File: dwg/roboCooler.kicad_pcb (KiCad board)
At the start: 2 copper layers, 36 parts, among them J1 CONN_02X25, J10 CONN_01X12, J11 CONN_01X12, J2 CONN_02X25, J3 CONN_01X04, J5 CONN_01X02, J7 CONN_01X02, Q1 NMOS, Q2 NMOS, Q3 NMOS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

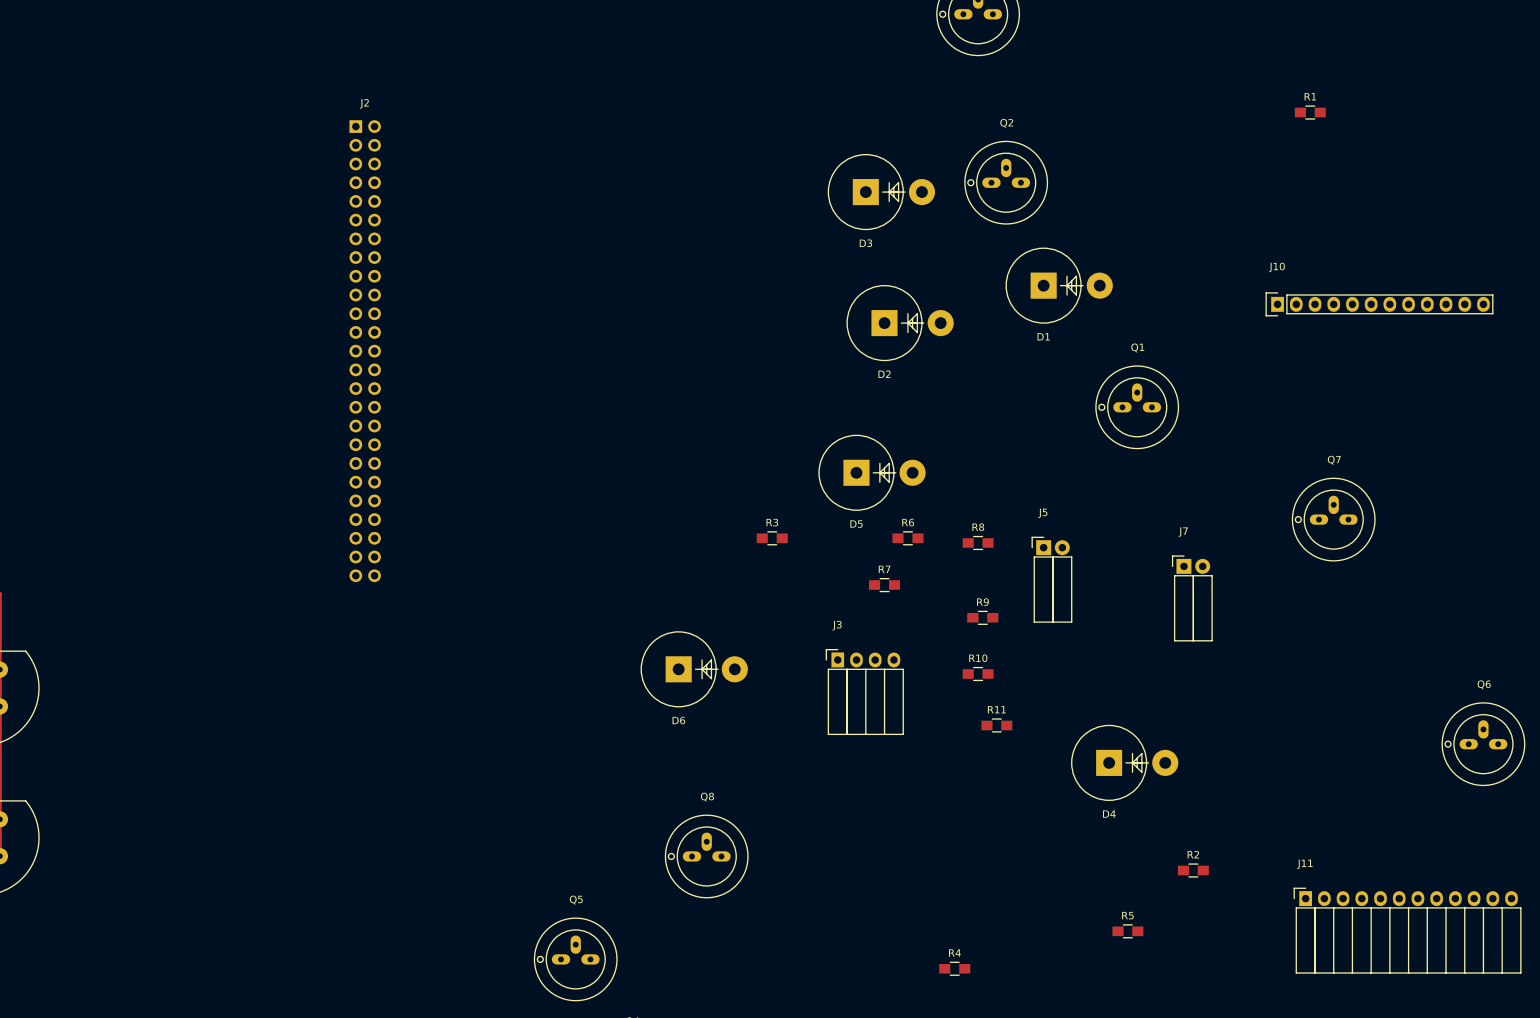
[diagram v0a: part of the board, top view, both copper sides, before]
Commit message: added cap sense to layout
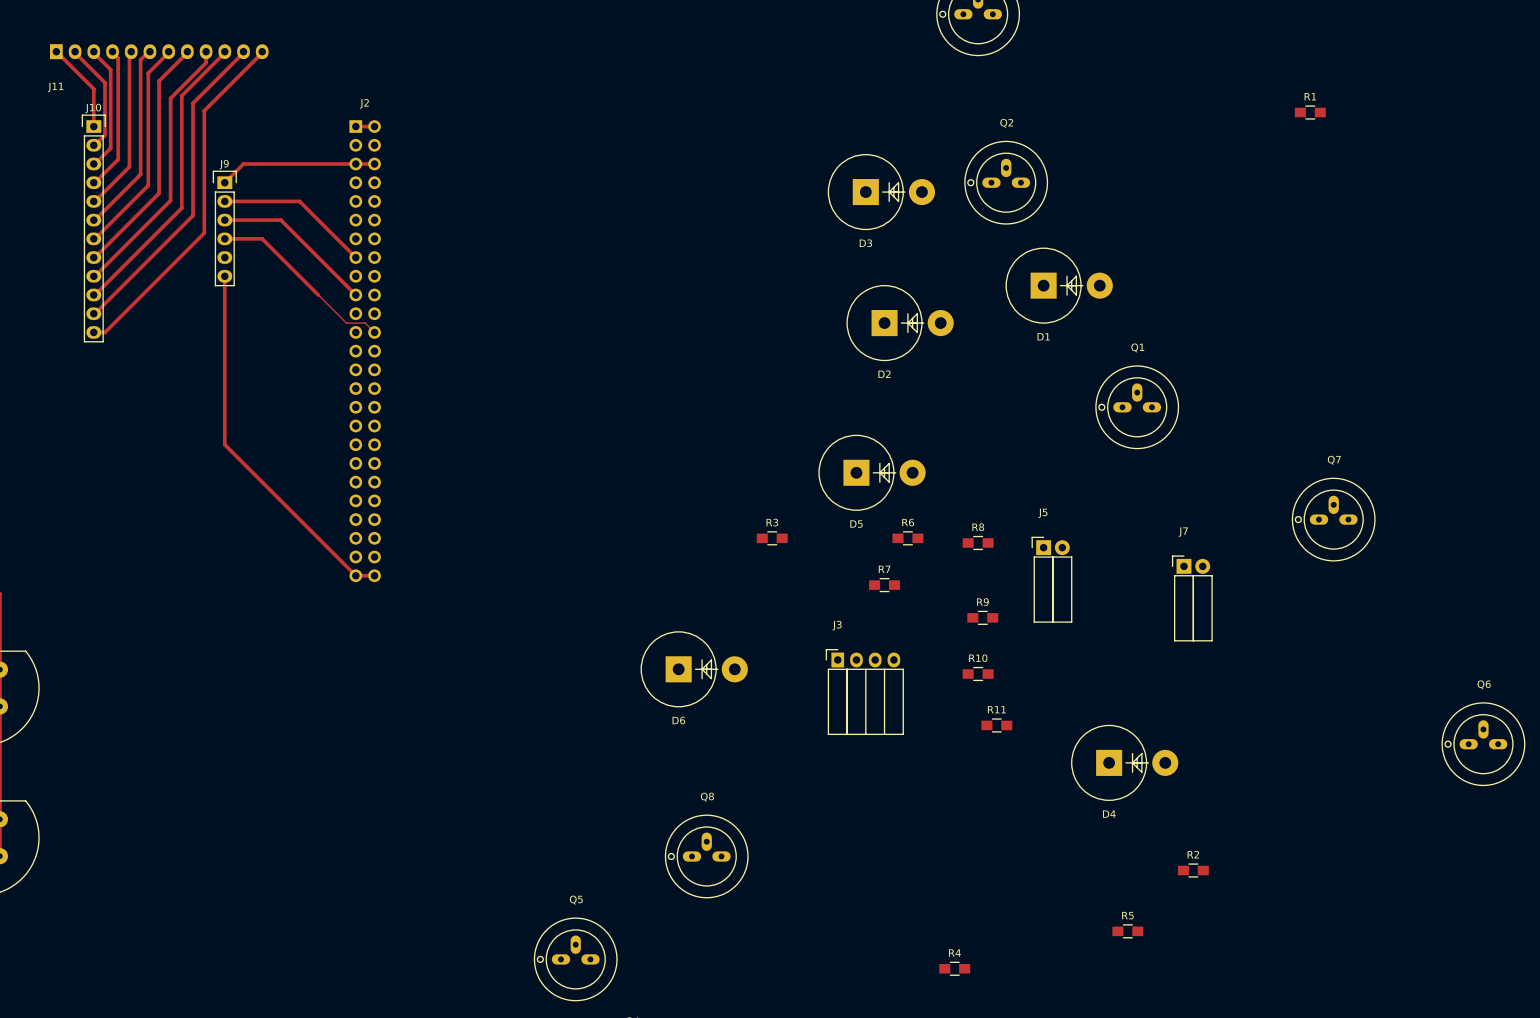
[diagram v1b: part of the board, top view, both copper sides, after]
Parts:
- added J9: CONN_01X06, Pin_Headers:Pin_Header_Straight_1x06, F.Cu at (99.1, 48.3)
- J11: moved to B.Cu
- moved J11 204.8 mm to (76.2, 30.5)
- moved J10 162.5 mm to (81.3, 40.6), turned to 270 degrees
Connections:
- J11 pad 1: Net-(J11-Pad1) -> CS_11
- J11 pad 10: Net-(J11-Pad10) -> CS_2
- J11 pad 11: Net-(J11-Pad11) -> CS_1
- J11 pad 12: Net-(J11-Pad12) -> CS_0
- J11 pad 2: Net-(J11-Pad2) -> CS_10
- J11 pad 3: Net-(J11-Pad3) -> CS_9
- J11 pad 4: Net-(J11-Pad4) -> CS_8
- J11 pad 5: Net-(J11-Pad5) -> CS_7
- J11 pad 6: Net-(J11-Pad6) -> CS_6
- J11 pad 7: Net-(J11-Pad7) -> CS_5
- J11 pad 8: Net-(J11-Pad8) -> CS_4
- J11 pad 9: Net-(J11-Pad9) -> CS_3
- J2 pad 15: Net-(J2-Pad15) -> CS_IRQ
- J2 pad 46: CS_IRQ -> Net-(J2-Pad46)
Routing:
- net POWER_GND: track 41.7 -> 94.8 mm
- net CS_0: track 0.00 -> 48.5 mm
- net CS_1: track 0.00 -> 44.1 mm
- net CS_2: track 0.00 -> 40.5 mm
- net CS_3: track 0.00 -> 36.9 mm
- net CS_4: track 0.00 -> 33.3 mm
- net CS_5: track 0.00 -> 29.7 mm
- net CS_6: track 0.00 -> 26.3 mm
- net CS_SDA: track 0.00 -> 25.6 mm
- net CS_7: track 0.00 -> 22.5 mm
- net CS_SCL: track 0.00 -> 22.0 mm
- net +3V3: track 0.00 -> 21.4 mm
- net CS_IRQ: track 0.00 -> 20.9 mm
- net CS_8: track 0.00 -> 19.6 mm
- net CS_9: track 0.00 -> 17.2 mm
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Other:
- net class BetweenPins added: clearance 0.2, trace_width 0.25, via_dia 0.6, via_drill 0.4

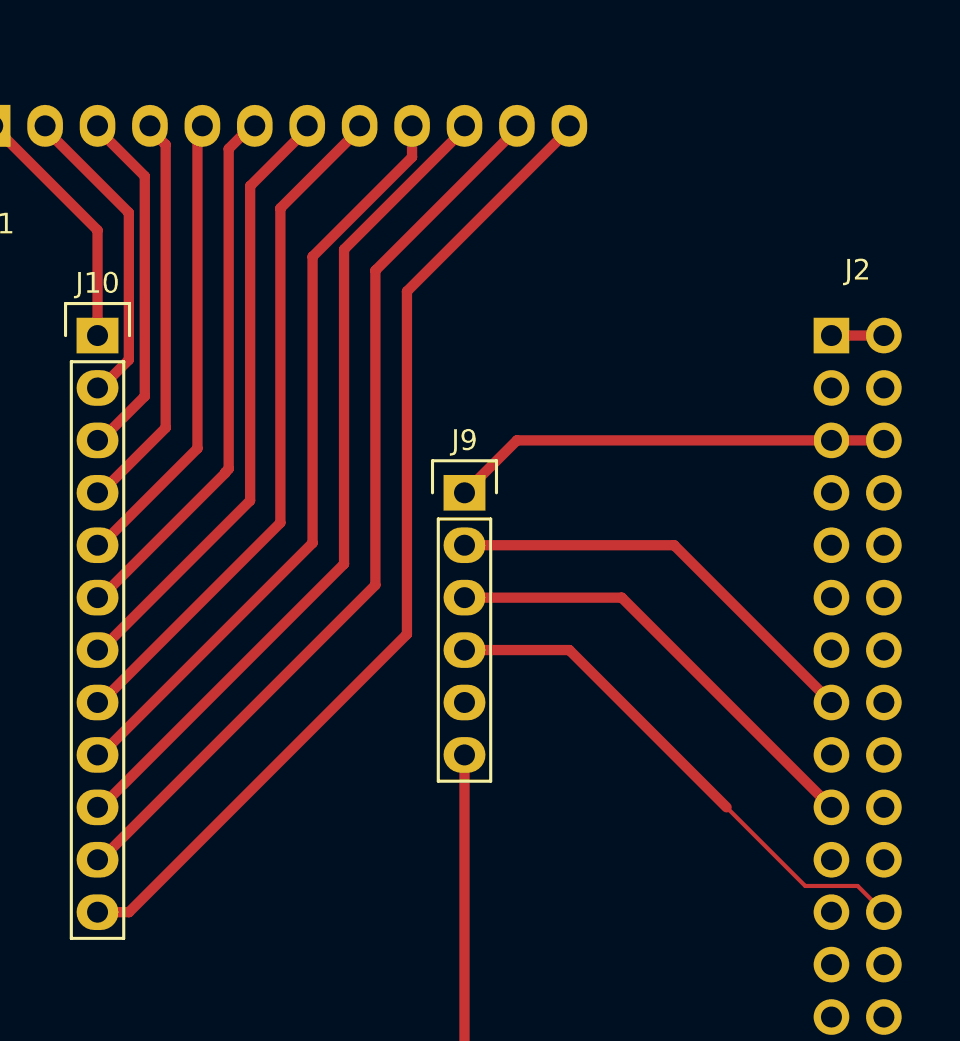
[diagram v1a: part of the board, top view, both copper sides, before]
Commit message: added pull up resistors to cap sense i2c lines
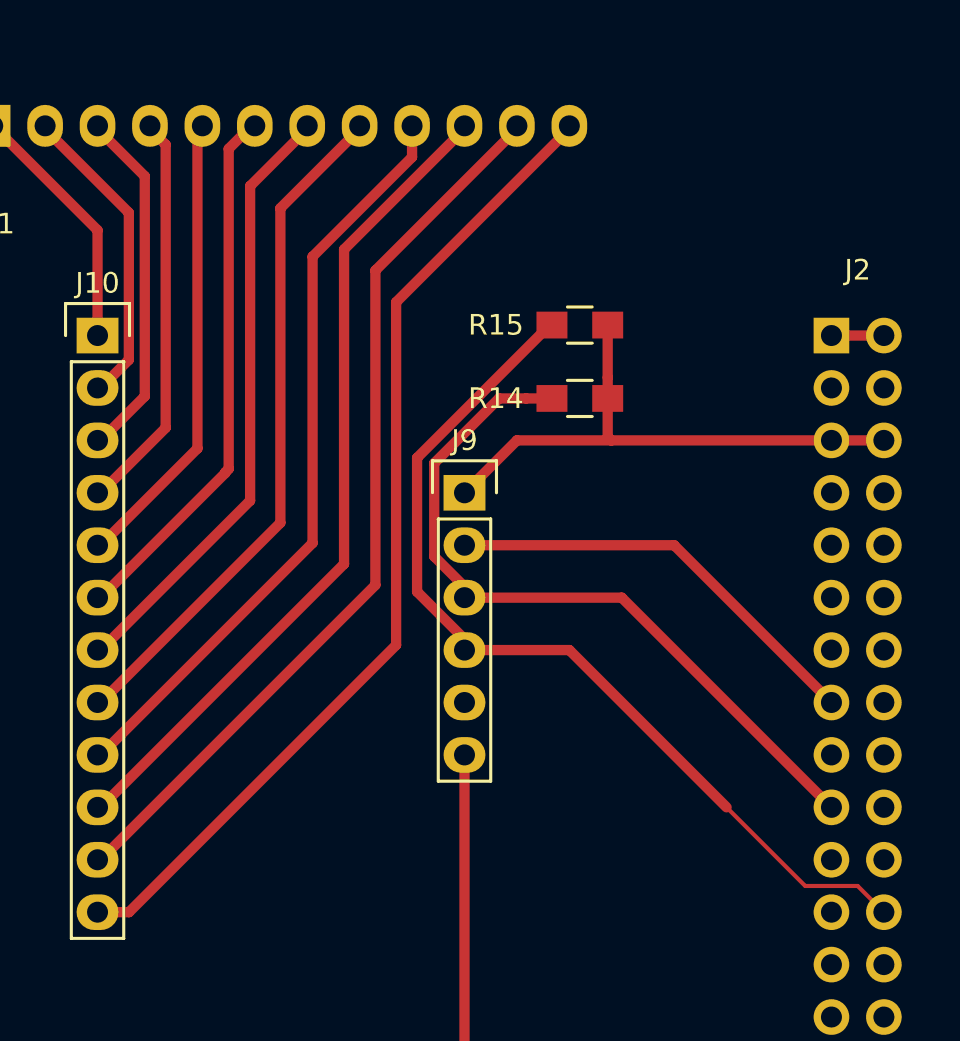
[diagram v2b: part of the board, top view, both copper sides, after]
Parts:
- added R14: 10k, Resistors_SMD:R_0805_HandSoldering, F.Cu at (104.6, 43.7)
- added R15: 10k, Resistors_SMD:R_0805_HandSoldering, F.Cu at (104.6, 40.1)
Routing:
- net CS_SDA: track 25.6 -> 45.0 mm
- net CS_SCL: track 22.0 -> 36.1 mm
- net +3V3: track 21.4 -> 27.0 mm
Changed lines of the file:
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@@
 (kicad_pcb (version 4) (host pcbnew 4.0.2-stable)
   (general
-    (links 87)
-    (no_connects 67)
+    (links 91)
+    (no_connects 58)
     (area 0 0 0 0)
     (thickness 1.6)
     (drawings 0)
-    (tracks 94)
+    (tracks 109)
     (zones 0)
-    (modules 37)
+    (modules 39)
     (nets 122)
   )
@@
     )
   )
+  (module Resistors_SMD:R_0805_HandSoldering (layer F.Cu)
+    (at 104.648 43.688 180)
+    (descr "Resistor SMD 0805, hand soldering")
+    (tags "resistor 0805")
+    (attr smd)
+    (fp_text reference R14 (at 4.064 0 180) (layer F.SilkS)
+      (effects (font (size 1 1) (thickness 0.15)))
+    )
+    (fp_text value 10k (at -4.064 0 180) (layer F.Fab)
+      (effects (font (size 1 1) (thickness 0.15)))
+    )
+    (fp_line (start -2.4 -1) (end 2.4 -1) (layer F.CrtYd) (width 0.05))
+    (fp_line (start -2.4 1) (end 2.4 1) (layer F.CrtYd) (width 0.05))
+    (fp_line (start -2.4 -1) (end -2.4 1) (layer F.CrtYd) (width 0.05))
+    (fp_line (start 2.4 -1) (end 2.4 1) (layer F.CrtYd) (width 0.05))
+    (fp_line (start 0.6 0.875) (end -0.6 0.875) (layer F.SilkS) (width 0.15))
+    (fp_line (start -0.6 -0.875) (end 0.6 -0.875) (layer F.SilkS) (width 0.15))
+    (pad 1 smd rect (at -1.35 0 180) (size 1.5 1.3) (layers F.Cu F.Paste F.Mask)
+      (net 49 +3V3))
+    (pad 2 smd rect (at 1.35 0 180) (size 1.5 1.3) (layers F.Cu F.Paste F.Mask)
+      (net 61 CS_SCL))
+    (model Resistors_SMD.3dshapes/R_0805_HandSoldering.wrl
+      (at (xyz 0 0 0))
+      (scale (xyz 1 1 1))
+      (rotate (xyz 0 0 0))
+    )
+  )
+  (module Resistors_SMD:R_0805_HandSoldering (layer F.Cu)
+    (at 104.648 40.132 180)
+    (descr "Resistor SMD 0805, hand soldering")
+    (tags "resistor 0805")
+    (attr smd)
+    (fp_text reference R15 (at 4.064 0 180) (layer F.SilkS)
+      (effects (font (size 1 1) (thickness 0.15)))
+    )
+    (fp_text value 10k (at -4.064 0 180) (layer F.Fab)
+      (effects (font (size 1 1) (thickness 0.15)))
+    )
+    (fp_line (start -2.4 -1) (end 2.4 -1) (layer F.CrtYd) (width 0.05))
+    (fp_line (start -2.4 1) (end 2.4 1) (layer F.CrtYd) (width 0.05))
+    (fp_line (start -2.4 -1) (end -2.4 1) (layer F.CrtYd) (width 0.05))
+    (fp_line (start 2.4 -1) (end 2.4 1) (layer F.CrtYd) (width 0.05))
+    (fp_line (start 0.6 0.875) (end -0.6 0.875) (layer F.SilkS) (width 0.15))
+    (fp_line (start -0.6 -0.875) (end 0.6 -0.875) (layer F.SilkS) (width 0.15))
+    (pad 1 smd rect (at -1.35 0 180) (size 1.5 1.3) (layers F.Cu F.Paste F.Mask)
+      (net 49 +3V3))
+    (pad 2 smd rect (at 1.35 0 180) (size 1.5 1.3) (layers F.Cu F.Paste F.Mask)
+      (net 65 CS_SDA))
+    (model Resistors_SMD.3dshapes/R_0805_HandSoldering.wrl
+      (at (xyz 0 0 0))
+      (scale (xyz 1 1 1))
+      (rotate (xyz 0 0 0))
+    )
+  )
   (segment (start 119.38 40.64) (end 116.84 40.64) (width 0.5) (layer F.Cu) (net 8))
   (segment (start 116.84 101.6) (end 119.38 101.6) (width 0.5) (layer F.Cu) (net 8))
@@
   (segment (start 63.5 43.18) (end 66.04 43.18) (width 0.5) (layer F.Cu) (net 9))
   (segment (start 50.8 105.33) (end 57.15 105.33) (width 0.5) (layer F.Cu) (net 9))
+  (segment (start 101.6 45.72) (end 106.172 45.72) (width 0.5) (layer F.Cu) (net 49))
+  (segment (start 105.998 42.672) (end 105.998 45.546) (width 0.5) (layer F.Cu) (net 49))
+  (segment (start 106.172 45.72) (end 116.84 45.72) (width 0.5) (layer F.Cu) (net 49))
+  (segment (start 105.998 45.546) (end 106.172 45.72) (width 0.5) (layer F.Cu) (net 49))
+  (segment (start 105.998 40.132) (end 105.998 42.672) (width 0.5) (layer F.Cu) (net 49))
   (segment (start 119.38 45.72) (end 116.84 45.72) (width 0.5) (layer F.Cu) (net 49))
-  (segment (start 101.6 45.72) (end 116.84 45.72) (width 0.5) (layer F.Cu) (net 49))
   (segment (start 99.06 48.26) (end 101.6 45.72) (width 0.5) (layer F.Cu) (net 49))
+  (segment (start 102.048 43.688) (end 103.298 43.688) (width 0.5) (layer F.Cu) (net 61))
+  (segment (start 100.731964 43.688) (end 102.048 43.688) (width 0.5) (layer F.Cu) (net 61))
+  (segment (start 99.06 52.810126) (end 97.593999 51.344125) (width 0.5) (layer F.Cu) (net 61))
+  (segment (start 99.06 53.34) (end 99.06 52.810126) (width 0.5) (layer F.Cu) (net 61))
+  (segment (start 97.593999 51.344125) (end 97.593999 46.825965) (width 0.5) (layer F.Cu) (net 61))
+  (segment (start 97.593999 46.825965) (end 100.731964 43.688) (width 0.5) (layer F.Cu) (net 61))
   (segment (start 99.06 53.34) (end 106.68 53.34) (width 0.5) (layer F.Cu) (net 61))
   (segment (start 106.68 53.34) (end 116.84 63.5) (width 0.5) (layer F.Cu) (net 61))
+  (segment (start 103.298 40.132) (end 103.198 40.132) (width 0.5) (layer F.Cu) (net 65))
+  (segment (start 103.198 40.132) (end 96.762824 46.567176) (width 0.5) (layer F.Cu) (net 65))
+  (segment (start 96.762824 46.567176) (end 96.762824 53.052949) (width 0.5) (layer F.Cu) (net 65))
+  (segment (start 96.762824 53.052949) (end 99.06 55.350125) (width 0.5) (layer F.Cu) (net 65))
+  (segment (start 99.06 55.350125) (end 99.06 55.88) (width 0.5) (layer F.Cu) (net 65))
   (segment (start 118.11 67.31) (end 115.57 67.31) (width 0.2) (layer F.Cu) (net 65))
   (segment (start 115.57 67.31) (end 111.76 63.5) (width 0.2) (layer F.Cu) (net 65))
@@
   (segment (start 81.4324 66.04) (end 81.28 66.04) (width 0.5) (layer F.Cu) (net 102))
   (segment (start 81.28 68.58) (end 82.804 68.58) (width 0.5) (layer F.Cu) (net 103))
-  (segment (start 82.804 68.58) (end 96.271278 55.112722) (width 0.5) (layer F.Cu) (net 103))
-  (segment (start 96.271278 55.112722) (end 96.271278 38.501122) (width 0.5) (layer F.Cu) (net 103))
-  (segment (start 96.271278 38.501122) (end 104.14 30.6324) (width 0.5) (layer F.Cu) (net 103))
+  (segment (start 95.746966 39.025434) (end 104.14 30.6324) (width 0.5) (layer F.Cu) (net 103))
+  (segment (start 82.804 68.58) (end 95.746966 55.637034) (width 0.5) (layer F.Cu) (net 103))
+  (segment (start 95.746966 55.637034) (end 95.746966 39.025434) (width 0.5) (layer F.Cu) (net 103))
   (segment (start 104.14 30.6324) (end 104.14 30.48) (width 0.5) (layer F.Cu) (net 103))
   (segment (start 63.54 119.34) (end 63.54 114.34) (width 0.5) (layer F.Cu) (net 115))

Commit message: added no connects to mcu connectors
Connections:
- J1 pad 18: FAN -> Net-(J1-Pad18)
- J2 pad 21: Net-(J2-Pad21) -> LED_UART
- J2 pad 23: LED_UART -> Net-(J2-Pad23)
